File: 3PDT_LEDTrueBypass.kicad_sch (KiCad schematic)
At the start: 9 parts, among them J1 Ground, J2 Effect Send, J3 Output, J4 Input, J5 Effect Return, J6 +9V, SW1 SW_3PDT

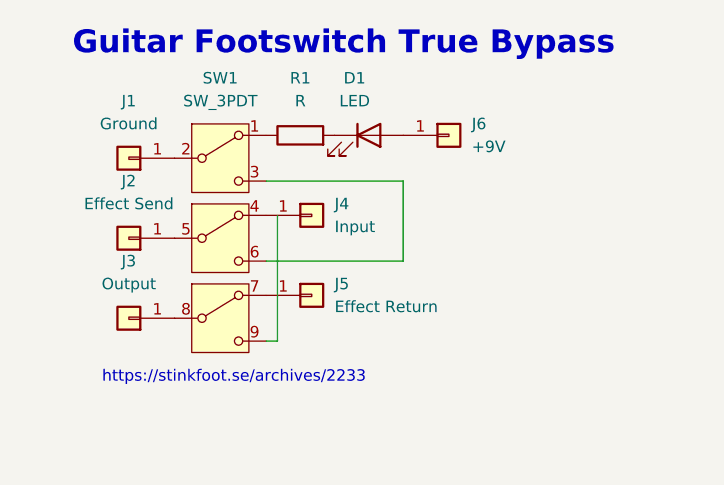
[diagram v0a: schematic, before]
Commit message: overhauled, rerouted and fixed pin spacings - vertical and horizontal spacings were mixed up
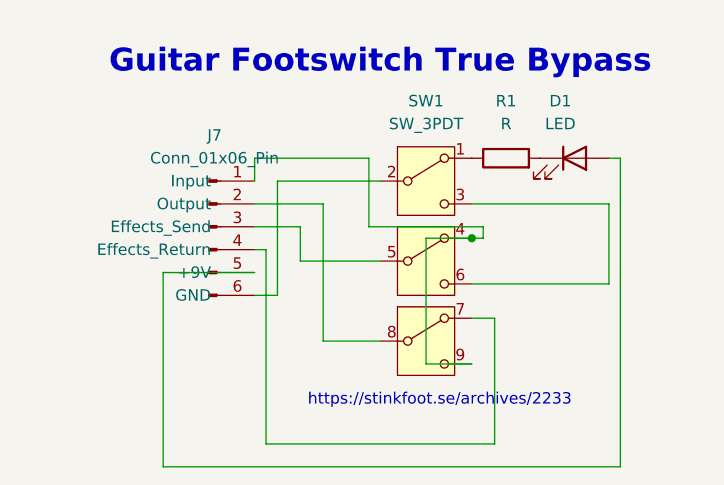
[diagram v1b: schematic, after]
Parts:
- removed J1: Ground, Connector_PinSocket_2.54mm:PinSocket_1x01_P2.54mm_Vertical, symbol Connector_Generic:Conn_01x01
- removed J2: Effect Send, Connector_PinSocket_2.54mm:PinSocket_1x01_P2.54mm_Vertical, symbol Connector_Generic:Conn_01x01
- removed J3: Output, Connector_PinSocket_2.54mm:PinSocket_1x01_P2.54mm_Vertical, symbol Connector_Generic:Conn_01x01
- removed J4: Input, Connector_PinSocket_2.54mm:PinSocket_1x01_P2.54mm_Vertical, symbol Connector_Generic:Conn_01x01
- removed J5: Effect Return, Connector_PinSocket_2.54mm:PinSocket_1x01_P2.54mm_Vertical, symbol Connector_Generic:Conn_01x01
- removed J6: +9V, Connector_PinSocket_2.54mm:PinSocket_1x01_P2.54mm_Vertical, symbol Connector_Generic:Conn_01x01
- added J7: Conn_01x06_Pin, Connector_PinHeader_2.54mm:PinHeader_1x06_P2.54mm_Vertical, symbol Connector:Conn_01x06_Pin
- D1: footprint LED_THT:LED_D3.0mm -> Connector_PinHeader_2.54mm:PinHeader_1x02_P2.54mm_Vertical
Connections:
- net at SW1.5 (E): now also J7.3 (Effects_Send)
- net at SW1.7 (G): now also J7.4 (Effects_Return)
- net at D1.2 (A): now also J7.5 (+9V)
- net at SW1.8 (H): now also J7.2 (Output)
- net at SW1.2 (B): now also J7.6 (GND)
- net at SW1.4 (D): now also SW1.9 (I), J7.1 (Input)
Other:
- moved on the sheet: D1, R1, SW1
